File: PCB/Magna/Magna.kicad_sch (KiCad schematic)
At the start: 0 parts

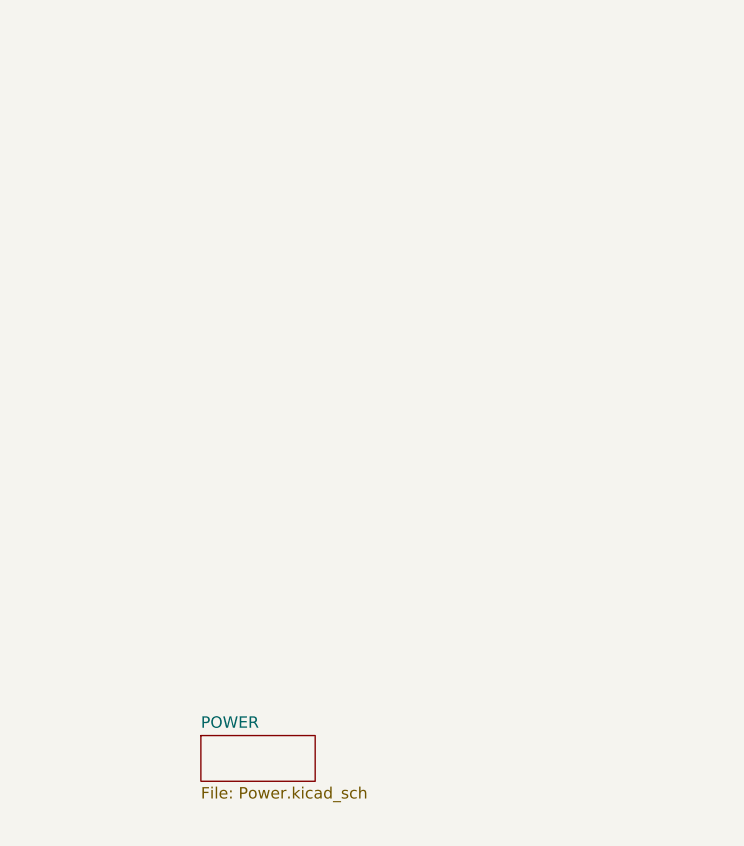
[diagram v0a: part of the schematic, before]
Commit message: Update analogue frontend and add potentiometer interface
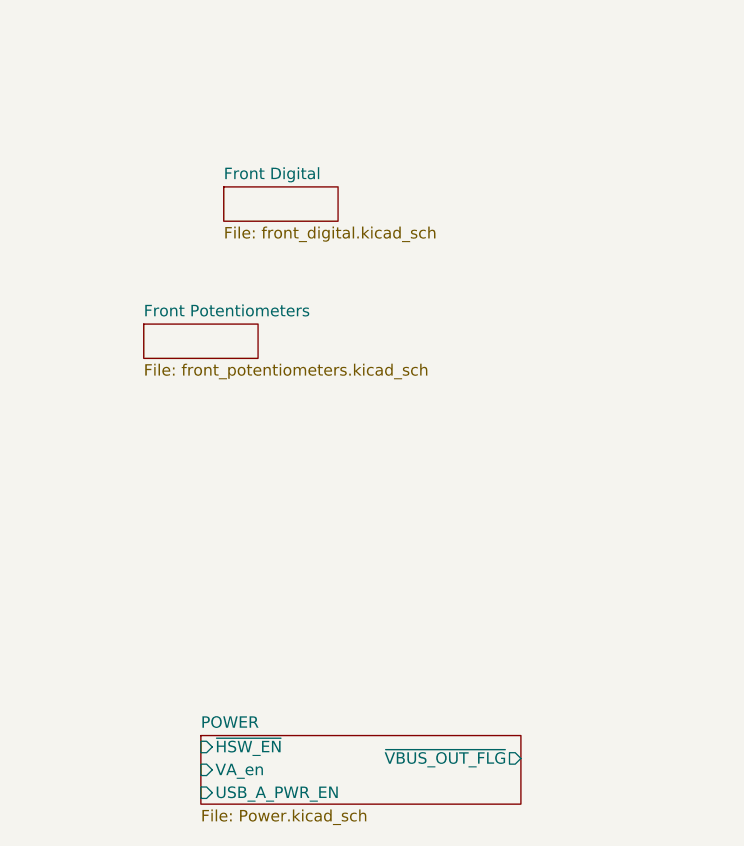
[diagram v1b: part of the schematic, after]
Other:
- added sheet Front Digital (front_digital.kicad_sch)
- added sheet Front Potentiometers (front_potentiometers.kicad_sch)
- sheet POWER ports: added USB_A_PWR_EN, VA_en, ~{HSW_EN}, ~{VBUS_OUT_FLG}; removed none
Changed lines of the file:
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@@
     (stroke (width 0) (type default))
   )
+  (sheet (at 43.18 114.3) (size 12.7 3.81) (fields_autoplaced)
+    (stroke (width 0.1524) (type solid))
+    (fill (color 0 0 0 0.0000))
+    (property "Sheetname" "Front Digital" (at 43.18 113.5884 0)
+      (effects (font (size 1.27 1.27)) (justify left bottom))
+    )
+    (property "Sheetfile" "front_digital.kicad_sch" (at 43.18 118.6946 0)
+      (effects (font (size 1.27 1.27)) (justify left top))
+    )
+    (instances
+      (project "Magna"
+        (path "/1469ea1f-a157-49dc-a369-2d42fa17695d" (page "18"))
+      )
+    )
+  )
   (sheet (at 40.64 59.69) (size 25.4 21.59) (fields_autoplaced)
     (stroke (width 0.1524) (type solid))
@@
     )
   )
-  (sheet (at 40.64 175.26) (size 12.7 5.08) (fields_autoplaced)
+  (sheet (at 40.64 175.26) (size 35.56 7.62) (fields_autoplaced)
     (stroke (width 0.1524) (type solid))
     (fill (color 0 0 0 0.0000))
@@
       (effects (font (size 1.27 1.27)) (justify left bottom))
     )
-    (property "Sheetfile" "Power.kicad_sch" (at 40.64 180.9246 0)
-      (effects (font (size 1.27 1.27)) (justify left top))
+    (property "Sheetfile" "Power.kicad_sch" (at 40.64 183.4646 0)
+      (effects (font (size 1.27 1.27)) (justify left top))
+    )
+    (pin "VA_en" input (at 40.64 179.07 180)
+      (effects (font (size 1.27 1.27)) (justify left))
+    )
+    (pin "~{HSW_EN}" input (at 40.64 176.53 180)
+      (effects (font (size 1.27 1.27)) (justify left))
+    )
+    (pin "USB_A_PWR_EN" input (at 40.64 181.61 180)
+      (effects (font (size 1.27 1.27)) (justify left))
+    )
+    (pin "~{VBUS_OUT_FLG}" output (at 76.2 177.8 0)
+      (effects (font (size 1.27 1.27)) (justify right))
     )
     (instances
@@
       )
     )
+  )
+  (sheet (at 34.29 129.54) (size 12.7 3.81) (fields_autoplaced)
+    (stroke (width 0.1524) (type solid))
+    (fill (color 0 0 0 0.0000))
+    (property "Sheetname" "Front Potentiometers" (at 34.29 128.8284 0)
+      (effects (font (size 1.27 1.27)) (justify left bottom))
+    )
+    (property "Sheetfile" "front_potentiometers.kicad_sch" (at 34.29 133.9346 0)
+      (effects (font (size 1.27 1.27)) (justify left top))
+    )
+    (property "Field2" "" (at 34.29 129.54 0)
+      (effects (font (size 1.27 1.27)) hide)
+    )
+    (instances
+      (project "Magna"
+        (path "/1469ea1f-a157-49dc-a369-2d42fa17695d" (page "14"))
+      )
+    )

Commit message: Add final touched to all schematics
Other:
- removed sheet Front Digital
- removed sheet Front Potentiometers
- added sheet Human Interface (human_interface.kicad_sch)
- sheet Audio IO ports: added {ADC_CONFIG}; removed ADC_CONFIG, BCLK_BUF
- sheet MCU ports: added CLK_24MHz, I2C_SCA, I2C_SCL, USB_A_PWR_EN, USB_OTG_FS_VBUS, VA_en, input_interrupt, {ADC_CONFIG}, {Output_Expander_bus}, {POT_BUS}, {USB_HS_ULPI}, {pot_select}, ~{HSW_EN}, ~{VBUS_OUT_FLG}; removed ADC_CONFIG, CLK_24MHZ, USB_HS_ULPI, ~{HOST_5V_EN}
- sheet USB ports: added USB_B_VBUS, {USB_HS_ULPI}; removed USB_HS_ULPI, ~{HOST_5V_EN}

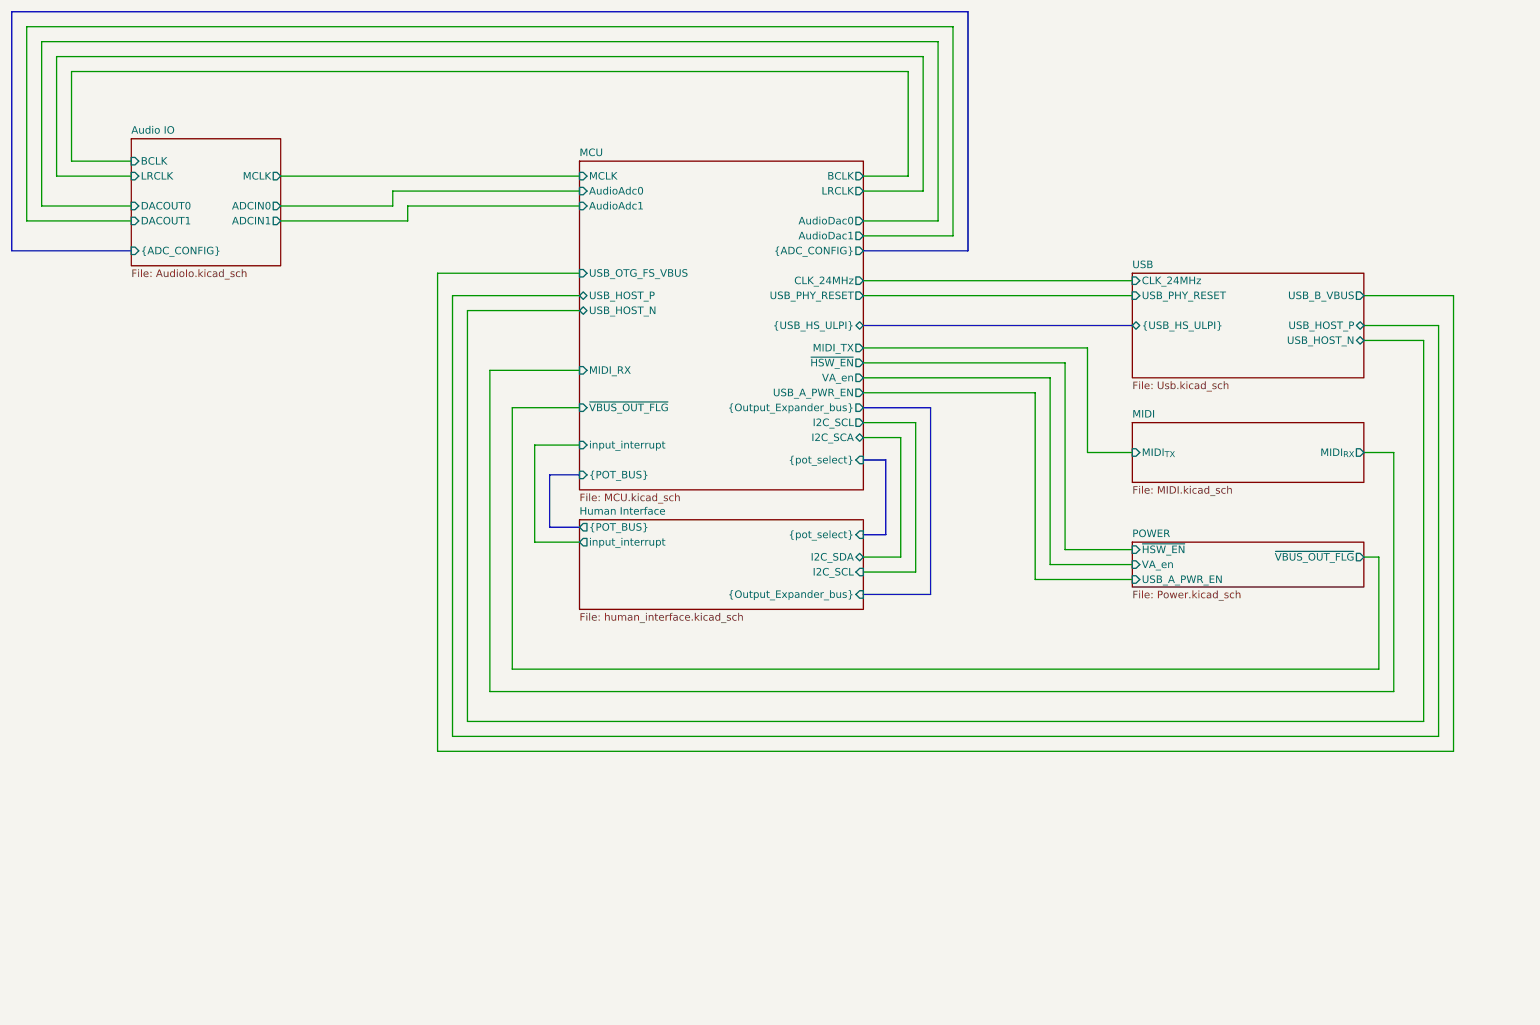
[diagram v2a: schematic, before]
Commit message: Remove all ERC in schematics
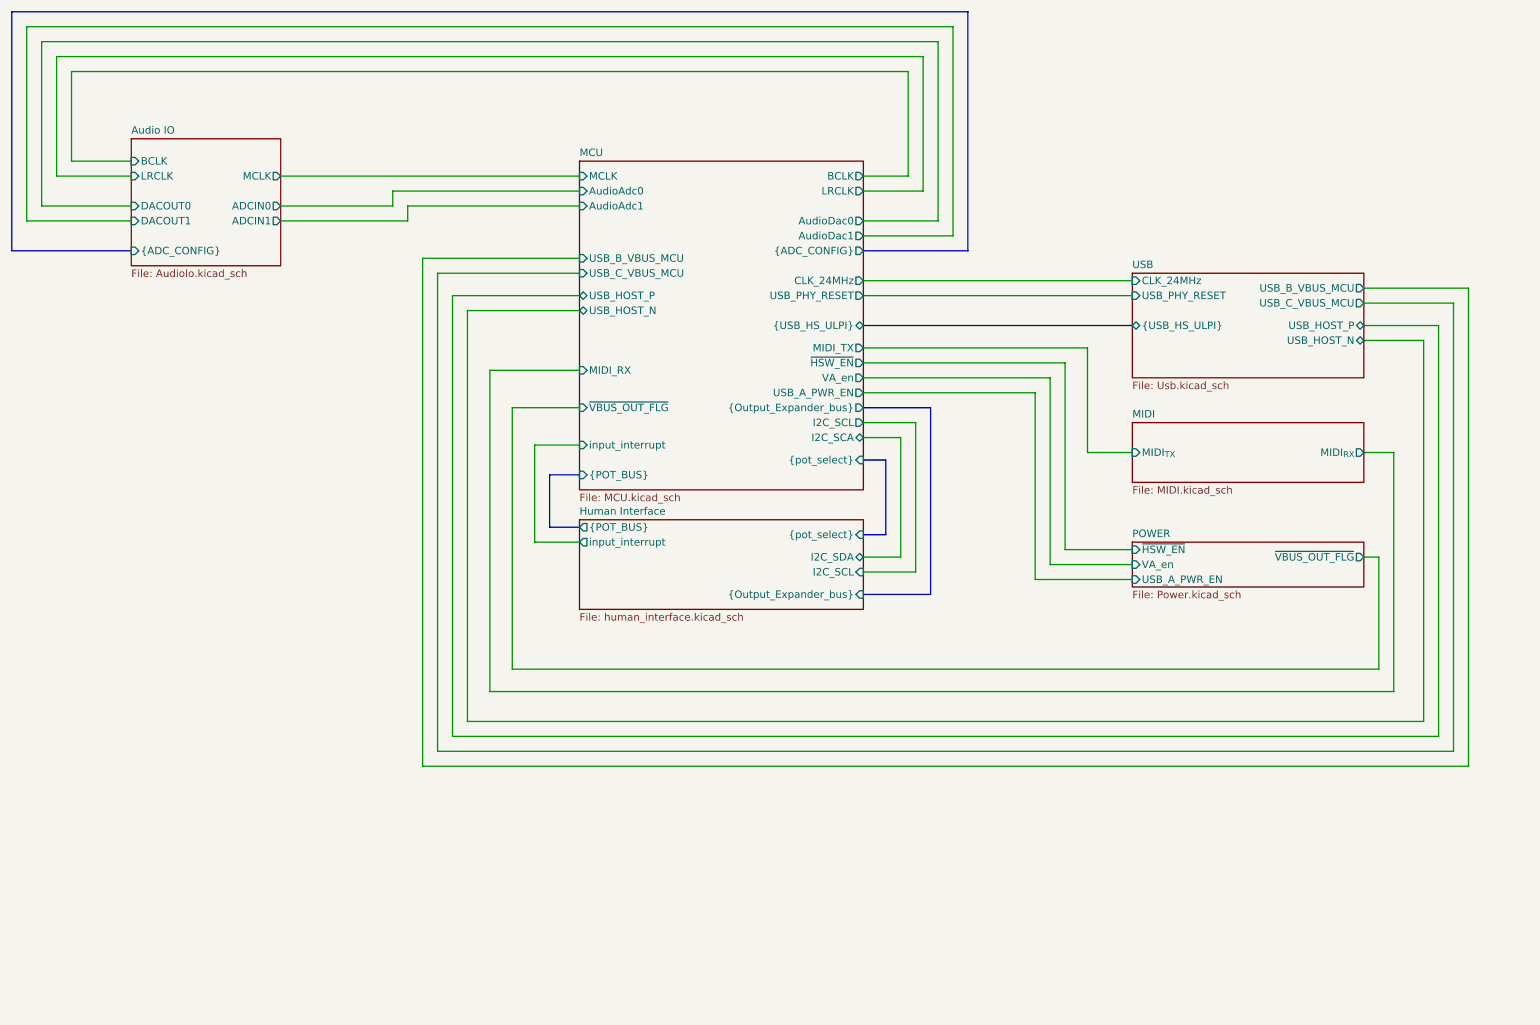
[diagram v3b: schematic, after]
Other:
- sheet MCU ports: added USB_B_VBUS_MCU, USB_C_VBUS_MCU; removed USB_OTG_FS_VBUS
- sheet USB ports: added USB_B_VBUS_MCU, USB_C_VBUS_MCU; removed USB_B_VBUS
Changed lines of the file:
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@@
+    (stroke (width 0) (type default))
+  )
+  (wire (pts (xy 266.7 62.23) (xy 248.92 62.23))
     (stroke (width 0) (type default))
   )
@@
     (stroke (width 0) (type default))
   )
+  (wire (pts (xy 115.57 57.15) (xy 88.9 57.15))
+    (stroke (width 0) (type default))
+  )
   (wire (pts (xy 163.83 107.95) (xy 170.18 107.95))
     (stroke (width 0) (type default))
@@
     (stroke (width 0) (type default))
   )
-  (wire (pts (xy 264.16 63.5) (xy 264.16 140.97))
+  (wire (pts (xy 264.16 64.77) (xy 264.16 140.97))
     (stroke (width 0) (type default))
   )
@@
     (stroke (width 0) (type default))
   )
+  (wire (pts (xy 88.9 57.15) (xy 88.9 143.51))
+    (stroke (width 0) (type default))
+  )
   (wire (pts (xy 163.83 60.96) (xy 209.55 60.96))
     (stroke (width 0) (type default))
@@
     (stroke (width 0) (type default))
   )
-  (wire (pts (xy 248.92 63.5) (xy 264.16 63.5))
+  (wire (pts (xy 248.92 64.77) (xy 264.16 64.77))
     (stroke (width 0) (type default))
   )
@@
     (stroke (width 0) (type default))
   )
+  (wire (pts (xy 266.7 143.51) (xy 266.7 62.23))
+    (stroke (width 0) (type default))
+  )
   (wire (pts (xy 173.99 22.86) (xy 173.99 45.72))
     (stroke (width 0) (type default))
@@
   )
   (wire (pts (xy 172.72 110.49) (xy 172.72 85.09))
+    (stroke (width 0) (type default))
+  )
+  (wire (pts (xy 88.9 143.51) (xy 266.7 143.51))
     (stroke (width 0) (type default))
   )
@@
       (effects (font (size 1.27 1.27)) (justify right))
     )
-    (pin "USB_OTG_FS_VBUS" input (at 115.57 59.69 180)
+    (pin "USB_C_VBUS_MCU" input (at 115.57 59.69 180)
+      (effects (font (size 1.27 1.27)) (justify left))
+    )
+    (pin "USB_B_VBUS_MCU" input (at 115.57 57.15 180)
       (effects (font (size 1.27 1.27)) (justify left))
     )
@@
       (effects (font (size 1.27 1.27)) (justify right))
     )
-    (pin "USB_B_VBUS" output (at 248.92 63.5 0)
-      (effects (font (size 1.27 1.27)) (justify right))
-    )
+    (pin "USB_B_VBUS_MCU" output (at 248.92 62.23 0)
+      (effects (font (size 1.27 1.27)) (justify right))
+    )
+    (pin "USB_C_VBUS_MCU" output (at 248.92 64.77 0)
+      (effects (font (size 1.27 1.27)) (justify right))
+    )

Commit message: Split schematic to several projects
To allow for several boards to be done a kicad project
is needed for each
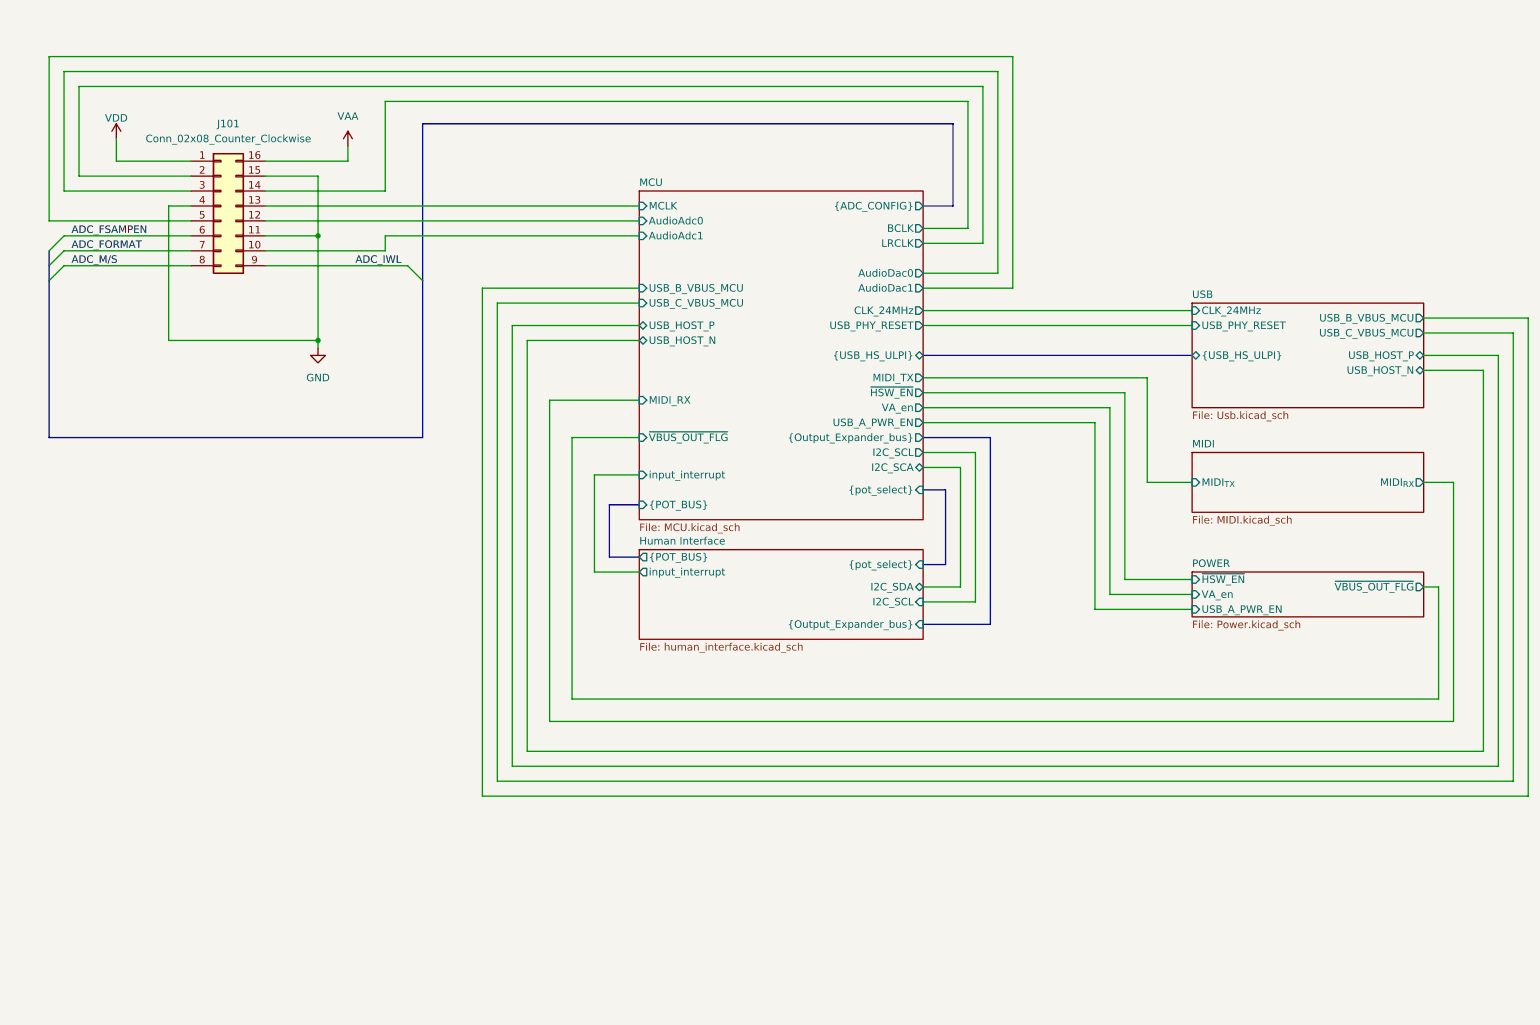
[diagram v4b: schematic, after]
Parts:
- added J101: Conn_02x08_Counter_Clockwise, Connector_PinSocket_2.54mm:PinSocket_2x08_P2.54mm_Vertical, symbol Connector_Generic:Conn_02x08_Counter_Clockwise
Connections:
- new net ADC_FORMAT: J101.7 (Pin_7)
- new net ADC_FSAMPEN: J101.6 (Pin_6)
- new net ADC_IWL: J101.9 (Pin_9)
- new net ADC_M/S: J101.8 (Pin_8)
- new net GND: J101.11 (Pin_11), J101.15 (Pin_15), J101.4 (Pin_4)
- new net MCU/AudioAdc0: J101.12 (Pin_12)
- new net MCU/AudioAdc1: J101.10 (Pin_10)
- new net MCU/AudioDac0: J101.3 (Pin_3)
- new net MCU/AudioDac1: J101.5 (Pin_5)
- new net MCU/BCLK: J101.14 (Pin_14)
- new net MCU/LRCLK: J101.2 (Pin_2)
- new net MCU/MCLK: J101.13 (Pin_13)
- new net VAA: J101.16 (Pin_16)
- new net VDD: J101.1 (Pin_1)
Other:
- removed sheet Audio IO
